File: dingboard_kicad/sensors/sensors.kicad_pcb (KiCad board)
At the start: 2 copper layers, 84.6 x 64 mm, 68 parts, among them J1 Bus_PCI_Express_x1, J2 TYPE-C-31-M-04, J3 Conn_01x02, U1 MCP25625T-E/ML, U2 RP2040, U3 TPS2121RUXR, U4 W25Q128JVP, U5 BMP388, U6 LMR51430 1.1k FPWM, U7 TPS63070RNMR, U8 BNO055, X1 ABM8-272-T3, Y1 ABS07-32.768KHZ-T

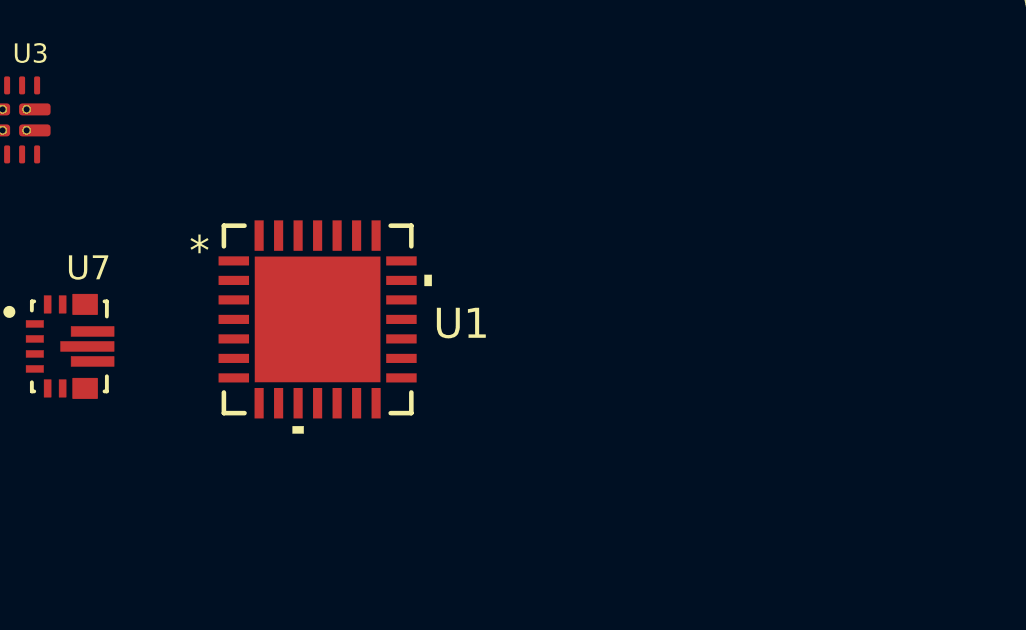
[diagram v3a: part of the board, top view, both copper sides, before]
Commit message: remove mux over volt protection
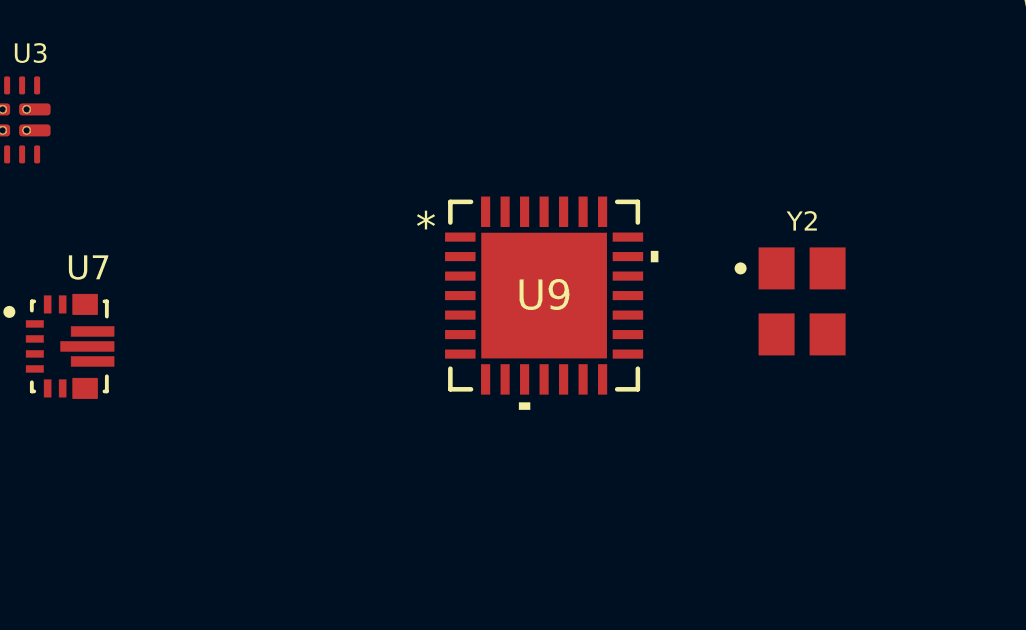
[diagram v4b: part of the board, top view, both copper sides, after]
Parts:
- removed U1: MCP25625T-E/ML, MCP25625:QFN28_6X6MC_MCH
- added U9: MCP25625T-E/ML, MCP25625:QFN28_6X6MC_MCH, F.Cu at (162.1, 79.7)
- added Y2: X322516MLB4SI, X322516MLB4SI:OSC_X322516MLB4SI, F.Cu at (170.7, 79.9)
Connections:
- J1 pad A8: unconnected-(J1-JTAG5-PadA8) -> CANL
- J1 pad A9: unconnected-(J1-+3.3V-PadA9) -> CANH
- J1 pad B8: unconnected-(J1-+3.3V-PadB8) -> CANL
- J1 pad B9: unconnected-(J1-JTAG1-PadB9) -> CANH
- U2 pad 11: unconnected-(U2-GPIO8-Pad11) -> BOOT_LOAD
- U2 pad 12: BOOT_LOAD -> unconnected-(U2-GPIO9-Pad12)
- U2 pad 14: unconnected-(U2-GPIO11-Pad14) -> SI
- U2 pad 15: unconnected-(U2-GPIO12-Pad15) -> SO
- U2 pad 16: unconnected-(U2-GPIO13-Pad16) -> CS
- U2 pad 17: unconnected-(U2-GPIO14-Pad17) -> SCK
- U2 pad 27: unconnected-(U2-GPIO16-Pad27) -> CANSTBY
- U2 pad 28: unconnected-(U2-GPIO17-Pad28) -> CANINT
- U2 pad 7: BNOINT -> unconnected-(U2-GPIO5-Pad7)
- U2 pad 8: unconnected-(U2-GPIO6-Pad8) -> BNOINT
